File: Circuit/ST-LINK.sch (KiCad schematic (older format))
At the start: 2 parts, among them P17 CONN_01X06

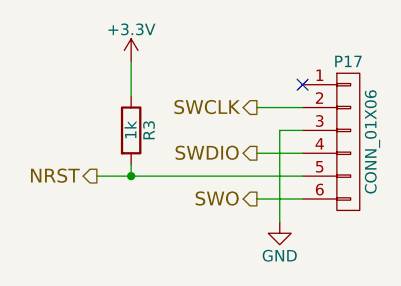
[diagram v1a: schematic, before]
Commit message: 部品割り付けの完了
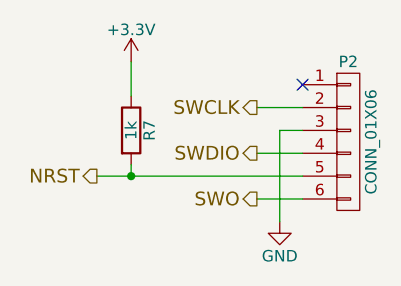
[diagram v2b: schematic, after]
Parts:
- renumbered P17 to P2, R3 to R7
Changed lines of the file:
@@
 LIBS:YASU
 LIBS:device
-LIBS:robocon_sch
 LIBS:rhand_controller-cache
 EELAYER 25 0
@@
 $EndDescr
 $Comp
-L CONN_01X06 P17
+L CONN_01X06 P2
 U 1 1 58DA469F
 P 3800 2850
-F 0 "P17" H 3800 3200 50  0000 C CNN
+F 0 "P2" H 3800 3200 50  0000 C CNN
 F 1 "CONN_01X06" V 3900 2850 50  0000 C CNN
 F 2 "Pin_Headers:Pin_Header_Straight_1x06_Pitch2.54mm" H 3800 2850 50  0001 C CNN
@@
 SWO
 $Comp
-L R R3
+L R R7
 U 1 1 593DD523
 P 2850 2800
-F 0 "R3" V 2930 2800 50  0000 C CNN
+F 0 "R7" V 2930 2800 50  0000 C CNN
 F 1 "1k" V 2850 2800 50  0000 C CNN
 F 2 "Resistors_SMD:R_0603_HandSoldering" V 2780 2800 50  0001 C CNN

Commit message: ADCのピン配置修正と配線引きはじめ
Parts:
- R7: footprint Resistors_SMD:R_0603_HandSoldering -> Resistors_ThroughHole:R_Axial_DIN0207_L6.3mm_D2.5mm_P7.62mm_Horizontal
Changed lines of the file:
@@
 LIBS:contrib
 LIBS:valves
-LIBS:YASU
 LIBS:device
+LIBS:robocon_sch
 LIBS:rhand_controller-cache
 EELAYER 25 0
@@
 F 0 "R7" V 2930 2800 50  0000 C CNN
 F 1 "1k" V 2850 2800 50  0000 C CNN
-F 2 "Resistors_SMD:R_0603_HandSoldering" V 2780 2800 50  0001 C CNN
+F 2 "Resistors_ThroughHole:R_Axial_DIN0207_L6.3mm_D2.5mm_P7.62mm_Horizontal" V 2780 2800 50  0001 C CNN
 F 3 "" H 2850 2800 50  0000 C CNN
 	1    2850 2800
